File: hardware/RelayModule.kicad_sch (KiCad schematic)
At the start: 2 parts, among them J9 Relay 1-4, U2 LTV-847S

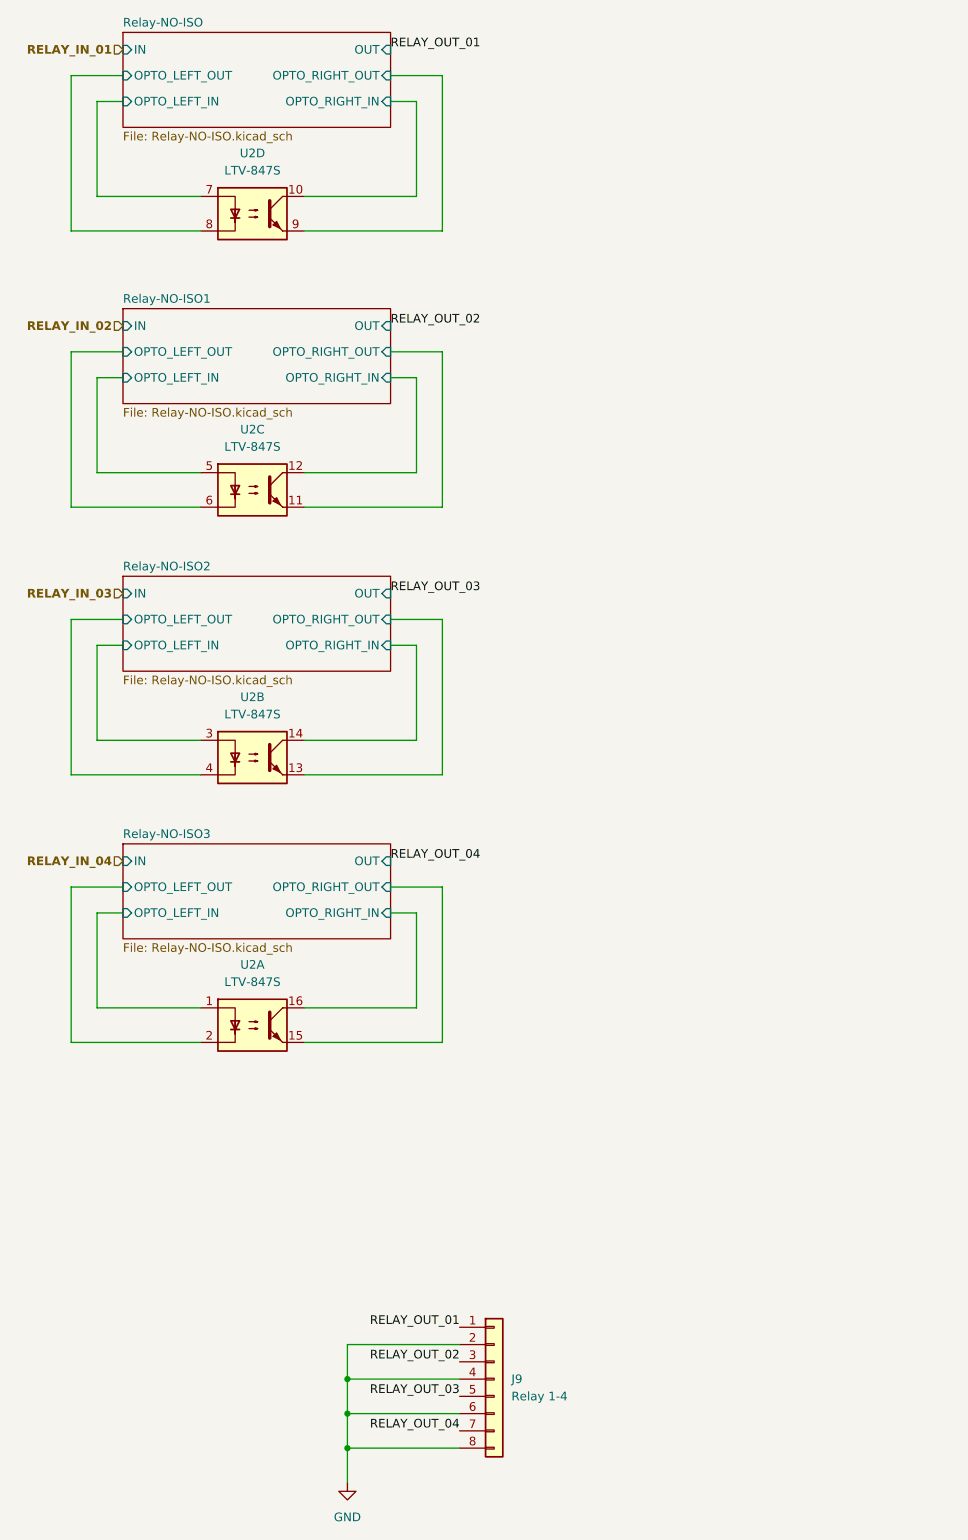
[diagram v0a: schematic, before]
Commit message: Transitioning to more robust circuit
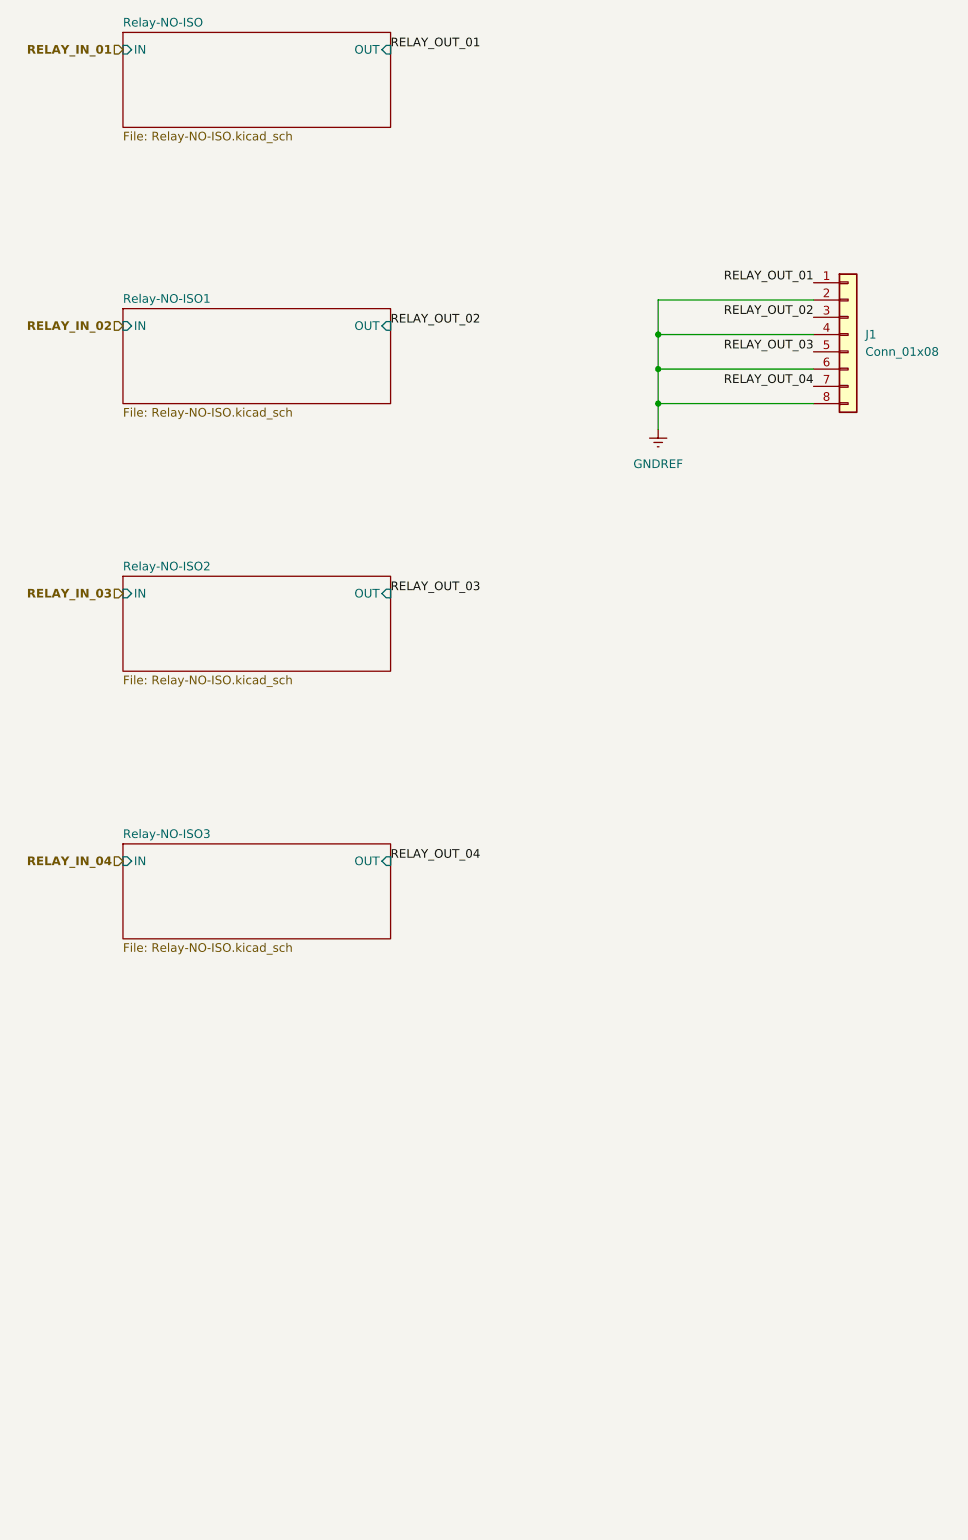
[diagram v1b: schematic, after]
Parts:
- removed J9: Relay 1-4, Connector_Phoenix_MSTB:PhoenixContact_MSTBA_2,5_8-G-5,08_1x08_P5.08mm_Horizontal, symbol Connector_Generic:Conn_01x08
- removed U2: LTV-847S, Package_DIP:SMDIP-16_W9.53mm, symbol Isolator:LTV-847S
- added J1: Conn_01x08, Header:PhoenixContact_MSTBA_2,5_8-G-5,08_1x08_P5.08mm_Horizontal, symbol Connector_Generic:Conn_01x08
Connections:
- net RELAY_OUT_01: now also J1.1 (Pin_1)
- net RELAY_OUT_02: now also J1.3 (Pin_3)
- net RELAY_OUT_03: now also J1.5 (Pin_5)
- net RELAY_OUT_04: now also J1.7 (Pin_7)
- new net GNDREF: J1.2 (Pin_2), J1.4 (Pin_4), J1.6 (Pin_6), J1.8 (Pin_8)
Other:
- sheet Relay-NO-ISO ports: added none; removed OPTO_LEFT_IN, OPTO_LEFT_OUT, OPTO_RIGHT_IN, OPTO_RIGHT_OUT
- sheet Relay-NO-ISO1 ports: added none; removed OPTO_LEFT_IN, OPTO_LEFT_OUT, OPTO_RIGHT_IN, OPTO_RIGHT_OUT
- sheet Relay-NO-ISO2 ports: added none; removed OPTO_LEFT_IN, OPTO_LEFT_OUT, OPTO_RIGHT_IN, OPTO_RIGHT_OUT
- sheet Relay-NO-ISO3 ports: added none; removed OPTO_LEFT_IN, OPTO_LEFT_OUT, OPTO_RIGHT_IN, OPTO_RIGHT_OUT

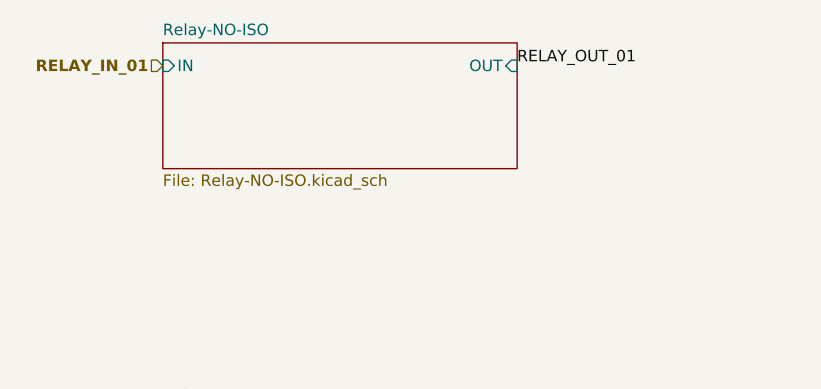
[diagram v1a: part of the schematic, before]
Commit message: It could work but it's too big
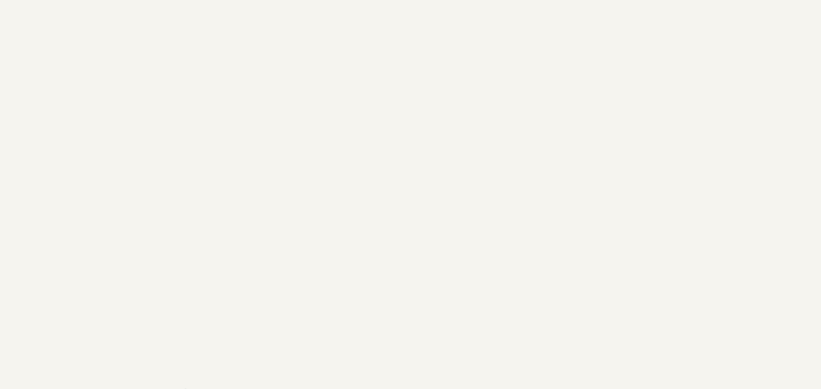
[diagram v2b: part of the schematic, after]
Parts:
- J1: footprint Header:PhoenixContact_MSTBA_2,5_8-G-5,08_1x08_P5.08mm_Horizontal -> Connector_Phoenix_MSTB:PhoenixContact_MSTBA_2,5_8-G-5,08_1x08_P5.08mm_Horizontal
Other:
- removed sheet Relay-NO-ISO
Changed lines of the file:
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@@
-		)
-	)
-	(label "RELAY_OUT_01"
-		(at 151.13 38.1 0)
-		(fields_autoplaced yes)
-		(effects
-			(font
-				(size 1.27 1.27)
-			)
-			(justify left bottom)
 		)
 	)
@@
 		(shape input)
 		(at 111.76 157.48 180)
-		(fields_autoplaced yes)
-		(effects
-			(font
-				(size 1.27 1.27)
-				(bold yes)
-			)
-			(justify right)
-		)
-	)
-	(hierarchical_label "RELAY_IN_01"
-		(shape input)
-		(at 111.76 38.1 180)
 		(fields_autoplaced yes)
 		(effects
@@
 			)
 		)
-		(property "Footprint" "Header:PhoenixContact_MSTBA_2,5_8-G-5,08_1x08_P5.08mm_Horizontal"
+		(property "Footprint" "Connector_Phoenix_MSTB:PhoenixContact_MSTBA_2,5_8-G-5,08_1x08_P5.08mm_Horizontal"
 			(at 218.44 80.01 0)
 			(effects
@@
 				)
 			)
-		)
-	)
-	(sheet
-		(at 111.76 35.56)
-		(size 39.37 13.97)
-		(fields_autoplaced yes)
-		(stroke
-			(width 0.1524)
-			(type solid)
-		)
-		(fill
-			(color 0 0 0 0.0000)
-		)
-		(property "Sheetname" "Relay-NO-ISO"
-			(at 111.76 34.8484 0)
-			(effects
-				(font
-					(size 1.27 1.27)
-				)
-				(justify left bottom)
-			)
-		)
-		(property "Sheetfile" "Relay-NO-ISO.kicad_sch"
-			(at 111.76 50.1146 0)
-			(effects
-				(font
-					(size 1.27 1.27)
-				)
-				(justify left top)
-			)
-		)
-		(pin "OUT" input
-			(at 151.13 38.1 0)
-			(effects
-				(font
-					(size 1.27 1.27)
-				)
-				(justify right)
-			)
-		)
-		(pin "IN" input
-			(at 111.76 38.1 180)
-			(effects
-				(font
-					(size 1.27 1.27)
-				)
-				(justify left)
-			)
-		)
-		(instances
-			(project "RS232-Relay"
-				(path "/6e416d74-c18a-4d9a-a47c-4314aa8f470f/6243990a-47f3-4383-9005-5094cba86ad2"
-					(page "5")
-				)
-				(path "/6e416d74-c18a-4d9a-a47c-4314aa8f470f/4cc60208-aa63-44fd-9447-92e9d40fbb60"
-					(page "6")
-				)
-				(path "/6e416d74-c18a-4d9a-a47c-4314aa8f470f/f5401bb4-9575-46b7-b322-a153ebcf6229"
-					(page "7")
-				)
-			)
